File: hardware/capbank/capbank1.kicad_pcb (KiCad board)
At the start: 2 copper layers, 91 x 64 mm, 134 parts, among them J1 Screws, J3 Conn_01x02, J4 Conn_01x02, J5 Conn_01x06, K1 3570.1333.121 COMUS, K2 3570.1333.121 COMUS, K4 3570.1333.121 COMUS, SW2 SW_SPST, U1 ULN2003, U10 TS861IL, U11 NXJ1S1212MC, U12 LM317AEMP, U13 74HC14, U14 MCP1415, U15 MCP1415, U16 LM78L05ACZ, U18 MCP4013-xxxxCH, U2 OPA2202IDR, U3 MCP1525-TO, U4 MCP4921-EP, U5 PAI130M61, U6 MCP6021T-E-OT, U7 74HC4046AD, U8 ATtiny84A-SS, U9 LM78L05ACZ, Y1 16MHz

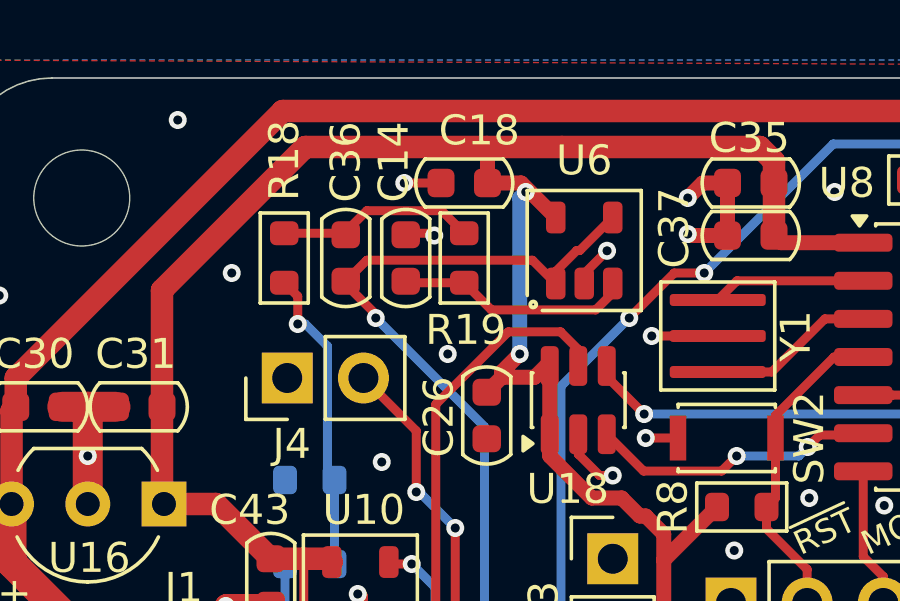
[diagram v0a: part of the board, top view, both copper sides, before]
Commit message: Update values after breadboard testing
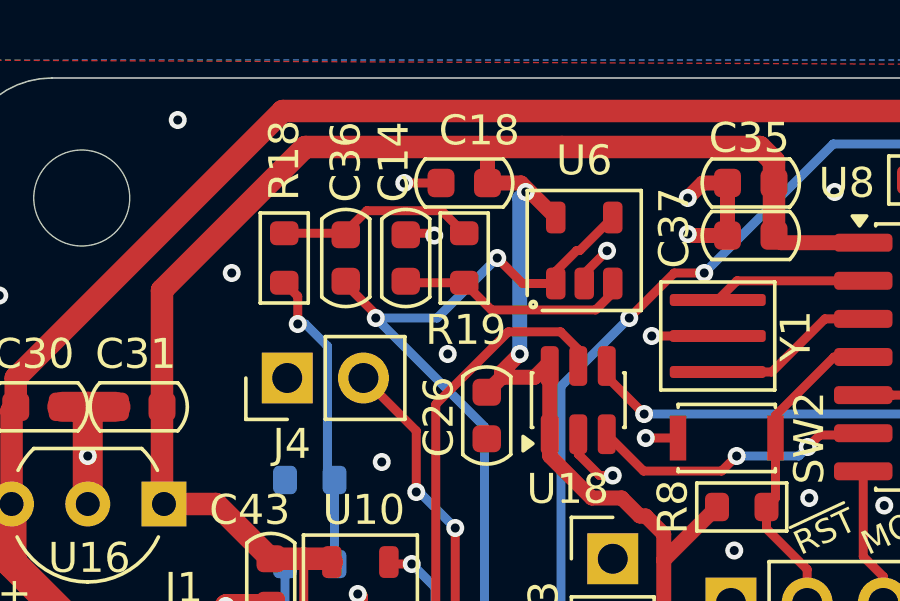
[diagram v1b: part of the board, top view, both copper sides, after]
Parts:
- R15: value 285k -> 470
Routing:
- net Net-(JP13-A): track 24.2 -> 23.7 mm, vias 1 -> 2
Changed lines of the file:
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@@
 			)
 		)
-		(property "Value" "285k"
+		(property "Value" "470"
 			(at 0 1.43 0)
 			(layer "F.Fab")
@@
 	)
 	(gr_line
-		(start 121.75 78.5)
-		(end 121.5 78.25)
+		(start 108.8 75.4)
+		(end 111.2 75)
 		(stroke
 			(width 0.1)
@@
 	)
 	(gr_line
-		(start 121.75 78.5)
-		(end 121.894871 78.174684)
+		(start 112 75.6)
+		(end 113 75)
 		(stroke
 			(width 0.1)
@@
 	)
 	(gr_line
-		(start 121.5 103.25)
-		(end 121.5 103.75)
+		(start 121 103.25)
+		(end 121.5 103.25)
 		(stroke
 			(width 0.1)
@@
 	)
 	(gr_line
-		(start 112 75.6)
-		(end 113 75)
+		(start 121 103.75)
+		(end 121.5 103.25)
 		(stroke
 			(width 0.1)
@@
 	)
 	(gr_line
-		(start 108.8 75.4)
-		(end 111.2 75)
+		(start 121.25 75.8)
+		(end 121.75 78.5)
 		(stroke
 			(width 0.1)
@@
 	)
 	(gr_line
-		(start 121.25 75.8)
-		(end 121.75 78.5)
+		(start 121.5 103.25)
+		(end 121.5 103.75)
 		(stroke
 			(width 0.1)
@@
 	)
 	(gr_line
-		(start 121 103.25)
-		(end 121.5 103.25)
+		(start 121.75 78.5)
+		(end 121.5 78.25)
 		(stroke
 			(width 0.1)
@@
 	)
 	(gr_line
-		(start 121 103.75)
-		(end 121.5 103.25)
+		(start 121.75 78.5)
+		(end 121.894871 78.174684)
 		(stroke
 			(width 0.1)
@@
 		(layer "F.SilkS")
 	)
-	(gr_line
-		(start 102 49)
-		(end 187 49)
+	(gr_arc
+		(start 99 52)
+		(mid 99.87868 49.87868)
+		(end 102 49)
 		(stroke
 			(width 0.05)
@@
 	)
 	(gr_line
-		(start 187 88)
-		(end 170 88)
-		(stroke
-			(width 0.05)
-			(type default)
-		)
-		(layer "Edge.Cuts")
-	)
-	(gr_arc
-		(start 187 49)
-		(mid 189.12132 49.87868)
-		(end 190 52)
+		(start 99 110)
+		(end 99 52)
 		(stroke
 			(width 0.05)
@@
 	)
 	(gr_line
-		(start 190 52)
-		(end 190 85)
+		(start 102 49)
+		(end 187 49)
 		(stroke
 			(width 0.05)
@@
 	)
 	(gr_arc
-		(start 190 85)
-		(mid 189.12132 87.12132)
-		(end 187 88)
+		(start 102 113)
+		(mid 99.87868 112.12132)
+		(end 99 110)
 		(stroke
 			(width 0.05)
@@
 		(layer "Edge.Cuts")
 	)
-	(gr_arc
-		(start 102 113)
-		(mid 99.87868 112.12132)
-		(end 99 110)
+	(gr_line
+		(start 164 113)
+		(end 102 113)
 		(stroke
 			(width 0.05)
@@
 		(layer "Edge.Cuts")
 	)
-	(gr_line
-		(start 164 113)
-		(end 102 113)
+	(gr_arc
+		(start 167 110)
+		(mid 166.12132 112.12132)
+		(end 164 113)
+		(stroke
+			(width 0.05)
+			(type default)
+		)
+		(layer "Edge.Cuts")
+	)
+	(gr_arc
+		(start 187 49)
+		(mid 189.12132 49.87868)
+		(end 190 52)
 		(stroke
 			(width 0.05)
@@
 	)
 	(gr_line
-		(start 99 110)
-		(end 99 52)
+		(start 187 88)
+		(end 170 88)
 		(stroke
 			(width 0.05)
@@
 		(layer "Edge.Cuts")
 	)
-	(gr_arc
-		(start 99 52)
-		(mid 99.87868 49.87868)
-		(end 102 49)
+	(gr_line
+		(start 190 52)
+		(end 190 85)
 		(stroke
 			(width 0.05)
@@
 	)
 	(gr_arc
-		(start 167 110)
-		(mid 166.12132 112.12132)
-		(end 164 113)
+		(start 190 85)
+		(mid 189.12132 87.12132)
+		(end 187 88)
 		(stroke
 			(width 0.05)
@@
 		(layer "Edge.Cuts")
 	)
-	(gr_text "~{RST}"
-		(at 127 65 25)
-		(layer "F.SilkS")
+	(gr_text "GND"
+		(at 123.5 69.5 0)
+		(layer "F.SilkS" knockout)
 		(effects
 			(font
@@
 		)
 	)
-	(gr_text "contact@tatjam.eu"
-		(at 122.25 89.75 0)
-		(layer "F.SilkS" knockout)
-		(effects
-			(font
-				(size 1.5 1.3)
-				(thickness 0.18)
-			)
-			(justify left bottom)
-		)
-	)
-	(gr_text "+"
-		(at 100.18 66.75 0)
+	(gr_text "~{RST}"
+		(at 127 65 25)
 		(layer "F.SilkS")
 		(effects
 			(font
-				(size 1 1)
+				(size 0.8 0.8)
 				(thickness 0.1)
 			)
@@
 		)
 	)
-	(gr_text "▲"
-		(at 123 70.75 90)
+	(gr_text "MISO"
+		(at 132.25 65 25)
 		(layer "F.SilkS")
 		(effects
 			(font
-				(size 1 1)
+				(size 0.8 0.8)
 				(thickness 0.1)
 			)
@@
 		)
 	)
-	(gr_text "MISO"
-		(at 132.25 65 25)
+	(gr_text "VDD"
+		(at 137.75 65 25)
 		(layer "F.SilkS")
 		(effects
@@
 		)
 	)
-	(gr_text "Varactor Board \nRev A"
-		(at 139.25 72.5 0)
+	(gr_text "+"
+		(at 100.18 66.75 0)
 		(layer "F.SilkS")
 		(effects
 			(font
-				(size 1.2 1.2)
-				(thickness 0.12)
+				(size 1 1)
+				(thickness 0.1)
 			)
 			(justify left bottom)
 		)
 	)
-	(gr_text "GND"
-		(at 123.5 69.5 0)
-		(layer "F.SilkS" knockout)
+	(gr_text "▲"
+		(at 123 70.75 90)
+		(layer "F.SilkS")
 		(effects
 			(font
-				(size 0.8 0.8)
+				(size 1 1)
 				(thickness 0.1)
 			)
@@
 		)
 	)
-	(gr_text "VDD"
-		(at 137.75 65 25)
+	(gr_text "Varactor Board \nRev A"
+		(at 139.25 72.5 0)
 		(layer "F.SilkS")
 		(effects
 			(font
-				(size 0.8 0.8)
-				(thickness 0.1)
+				(size 1.2 1.2)
+				(thickness 0.12)
+			)
+			(justify left bottom)
+		)
+	)
+	(gr_text "contact@tatjam.eu"
+		(at 122.25 89.75 0)
+		(layer "F.SilkS" knockout)
+		(effects
+			(font
+				(size 1.5 1.3)
+				(thickness 0.18)
 			)
 			(justify left bottom)
@@
 	)
 	(segment
-		(start 112.501 55.074)
-		(end 118.024 55.074)
+		(start 117.7 55.85)
+		(end 116.85 55)
 		(width 0.3)
 		(layer "F.Cu")
@@
 	)
 	(segment
-		(start 111.75 55.825)
-		(end 112.501 55.074)
-		(width 0.3)
-		(layer "F.Cu")
-		(net 77)
-	)
-	(segment
 		(start 118.8 55.45)
 		(end 118.8 55.85)
@@
 	)
 	(segment
-		(start 118.024 55.074)
-		(end 118.8 55.85)
+		(start 118.8 55.85)
+		(end 117.7 55.85)
 		(width 0.3)
 		(layer "F.Cu")
@@
 	)
 	(via
+		(at 116.85 55)
+		(size 0.6)
+		(drill 0.3)
+		(layers "F.Cu" "B.Cu")
+		(net 77)
+	)
+	(via
 		(at 112.8 57)
 		(size 0.6)
@@
 	)
 	(segment
+		(start 116.85 55)
+		(end 114.85 57)
+		(width 0.3)
+		(layer "B.Cu")
+		(net 77)
+	)
+	(segment
 		(start 116.425 67.4)
 		(end 116.425 60.625)
 		(width 0.3)
 		(layer "B.Cu")
+		(net 77)
+	)
+	(segment
+		(start 114.85 57)
+		(end 112.8 57)
+		(width 0.3)
+		(layer "B.Cu")

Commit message: Getting ready for manufacture
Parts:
- added C38: 80pF, PCM_Capacitor_SMD_AKL:C_0603_1608Metric, F.Cu at (170.4, 66.4)
- added R21: 2.8k, PCM_Resistor_SMD_AKL:R_1206_3216Metric_Pad1.30x1.75mm_HandSolder, B.Cu at (149.8, 104.4)
- added R32: 3.3k, PCM_Resistor_SMD_AKL:R_1206_3216Metric_Pad1.30x1.75mm_HandSolder, B.Cu at (150.8, 97.4)
- C27: footprint PCM_Capacitor_THT_AKL:CP_Radial_D8.0mm_P3.50mm -> PCM_Capacitor_THT_AKL:CP_Radial_D6.3mm_P2.50mm
- FB1: value Ferrite_Bead -> BLM18PG121SN1D
- J1: value Screws -> XY308-2P 2.54MM
- R20, R27, R28, R29, R30, R31: value 22M -> 10M
- R23: value 7k -> 3.3k; footprint PCM_Resistor_SMD_AKL:R_1812_4532Metric -> PCM_Resistor_SMD_AKL:R_1206_3216Metric_Pad1.30x1.75mm_HandSolder
- R7: value 5.6k -> 2.8k; footprint PCM_Resistor_SMD_AKL:R_1210_3225Metric_Pad1.30x2.65mm_HandSolder -> PCM_Resistor_SMD_AKL:R_1206_3216Metric_Pad1.30x1.75mm_HandSolder
- U14, U15: value MCP1415 -> FAN3111E
- moved U15 7.08 mm to (119.8, 99.9)
- moved U14 5.64 mm to (119.6, 106.6)
- moved D1 0.77 mm to (167.8, 66.3)
- moved D2 0.77 mm to (164.8, 66.3)
- moved D3 0.77 mm to (161.8, 66.3)
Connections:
- R23 pad 2: GND_ISOL -> Net-(R23-Pad2)
- R7 pad 2: GND_ISOL -> Net-(R21-Pad1)
- U14 pad 1: unconnected-(U14-NC-Pad1) -> /BiasSupply/SWITCH_SUPPLY
- U14 pad 2: /BiasSupply/SWITCH_SUPPLY -> GND_ISOL
- U14 pad 3: /BiasSupply/OSC -> /BiasSupply/~{OSC}
- U14 pad 4: GND_ISOL -> VDD_ISOL
- U14 pad 5: /BiasSupply/~{DRIVE} -> /BiasSupply/DRIVE
- U15 pad 1: unconnected-(U15-NC-Pad1) -> /BiasSupply/SWITCH_SUPPLY
- U15 pad 2: /BiasSupply/SWITCH_SUPPLY -> GND_ISOL
- U15 pad 3: /BiasSupply/~{OSC} -> /BiasSupply/OSC
- U15 pad 4: GND_ISOL -> VDD_ISOL
- U15 pad 5: /BiasSupply/DRIVE -> /BiasSupply/~{DRIVE}
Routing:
- net VDD_ISOL: track 100.0 -> 116.0 mm
- net Net-(R21-Pad1): track 0.00 -> 3.71 mm
- net Net-(R23-Pad2): track 0.00 -> 2.99 mm
- net Net-(D1-K): track 14.8 -> 17.6 mm
- net /BiasSupply/SWITCH_SUPPLY: track 30.7 -> 33.1 mm, vias 0 -> 4
- net GND_ISOL: track 138.7 -> 140.9 mm, vias 47 -> 46
- net /Isolated/Varactor/VBIAS: track 10.3 -> 9.27 mm
- net /BiasSupply/OSC: track 18.7 -> 18.0 mm
- net /BiasSupply/~{OSC}: track 13.2 -> 12.5 mm

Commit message: Getting nearer to prod
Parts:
- removed U18: MCP4013-xxxxCH, Package_TO_SOT_SMD:SOT-23-6
- added R33: 50k, PCM_Resistor_SMD_AKL:R_0603_1608Metric, F.Cu at (117.8, 66.9)
- added R34: 50k, PCM_Resistor_SMD_AKL:R_0603_1608Metric, F.Cu at (117.8, 63.5)
- added U17: MCP4012-503ECH, Package_TO_SOT_SMD:SOT-23-6, F.Cu at (119.5, 59.7)
- C11, C12: value 10n -> 10n low esr
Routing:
- net Net-(D1-K): track 17.6 -> 3.76 mm
- net GND_ISOL: track 140.9 -> 132.1 mm, vias 46 -> 59
- net Net-(U17-W): track 16.7 -> 22.4 mm
- net VDD: track 163.8 -> 165.4 mm
- net GND: track 75.1 -> 75.9 mm, vias 59 -> 61
- net (no net): vias 0 -> 15
